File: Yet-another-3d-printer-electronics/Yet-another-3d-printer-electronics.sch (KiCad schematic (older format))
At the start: 14 parts, among them CON1 SD_Card, P2 BEDTEMP, P3 ENDTEMP, SW1 Switch_DPST, U2 LPC1114FBD48/302, X1 CRYSTAL_SMD

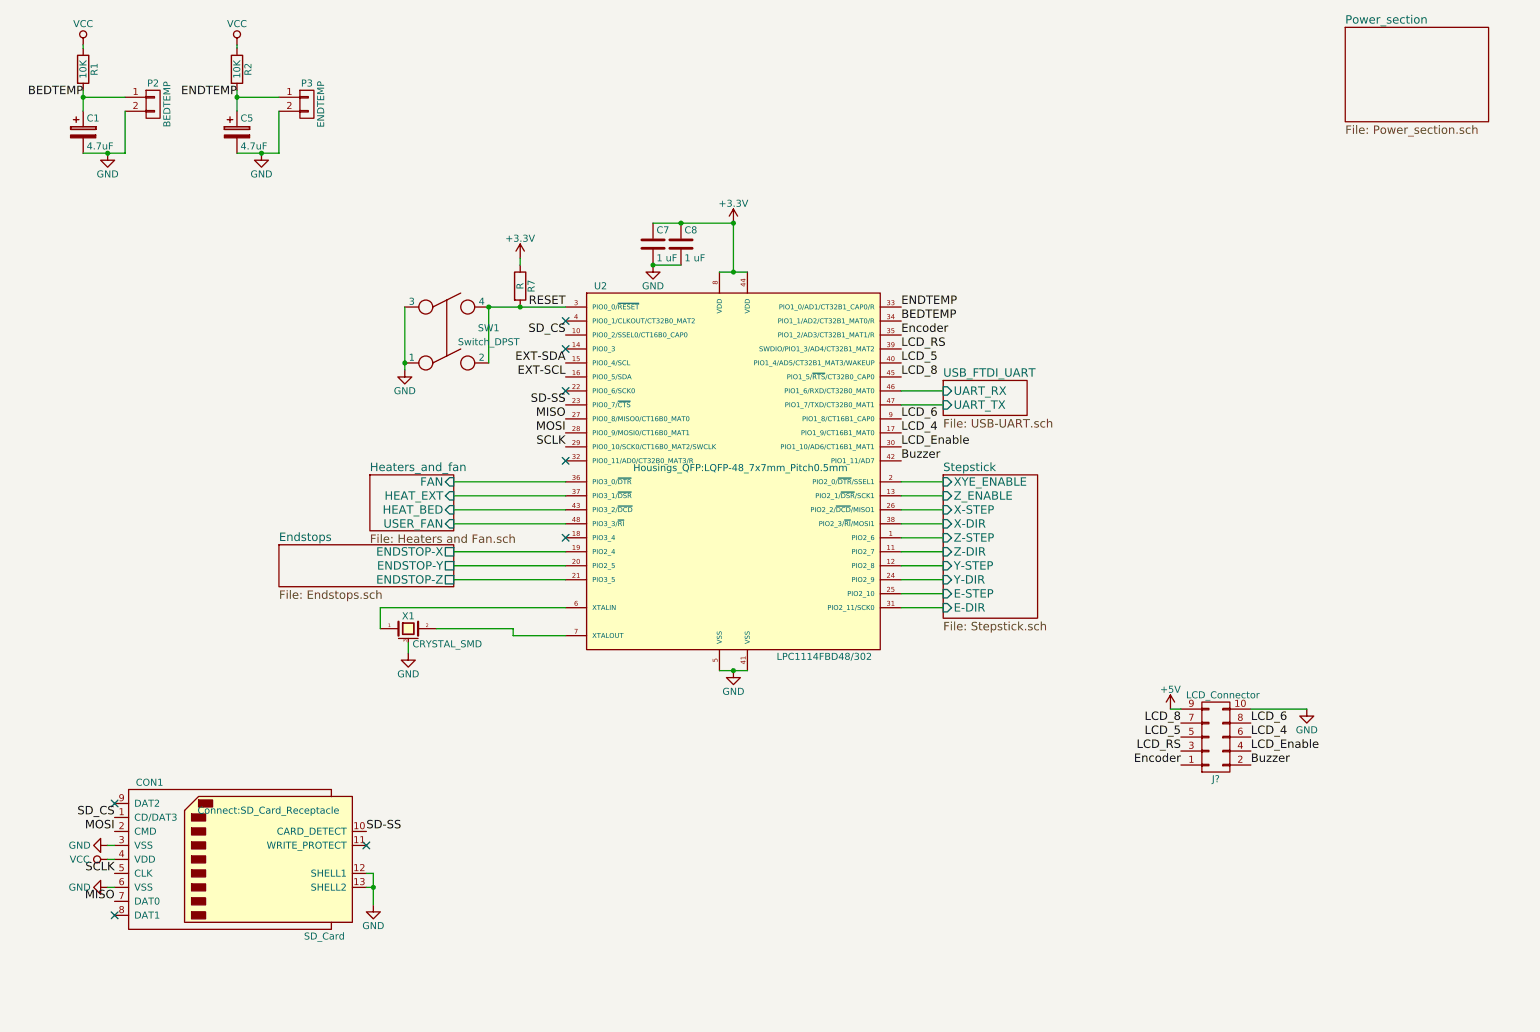
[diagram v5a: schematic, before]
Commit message: Add additional stepstick, hotend fan and heater and temperature sensor
Extruder stepsticks have independ enables pins. Vcc was replace by valid
power source.

Signed-off-by: Mateusz Krawczuk <mat.krawczuk@gmail.com>
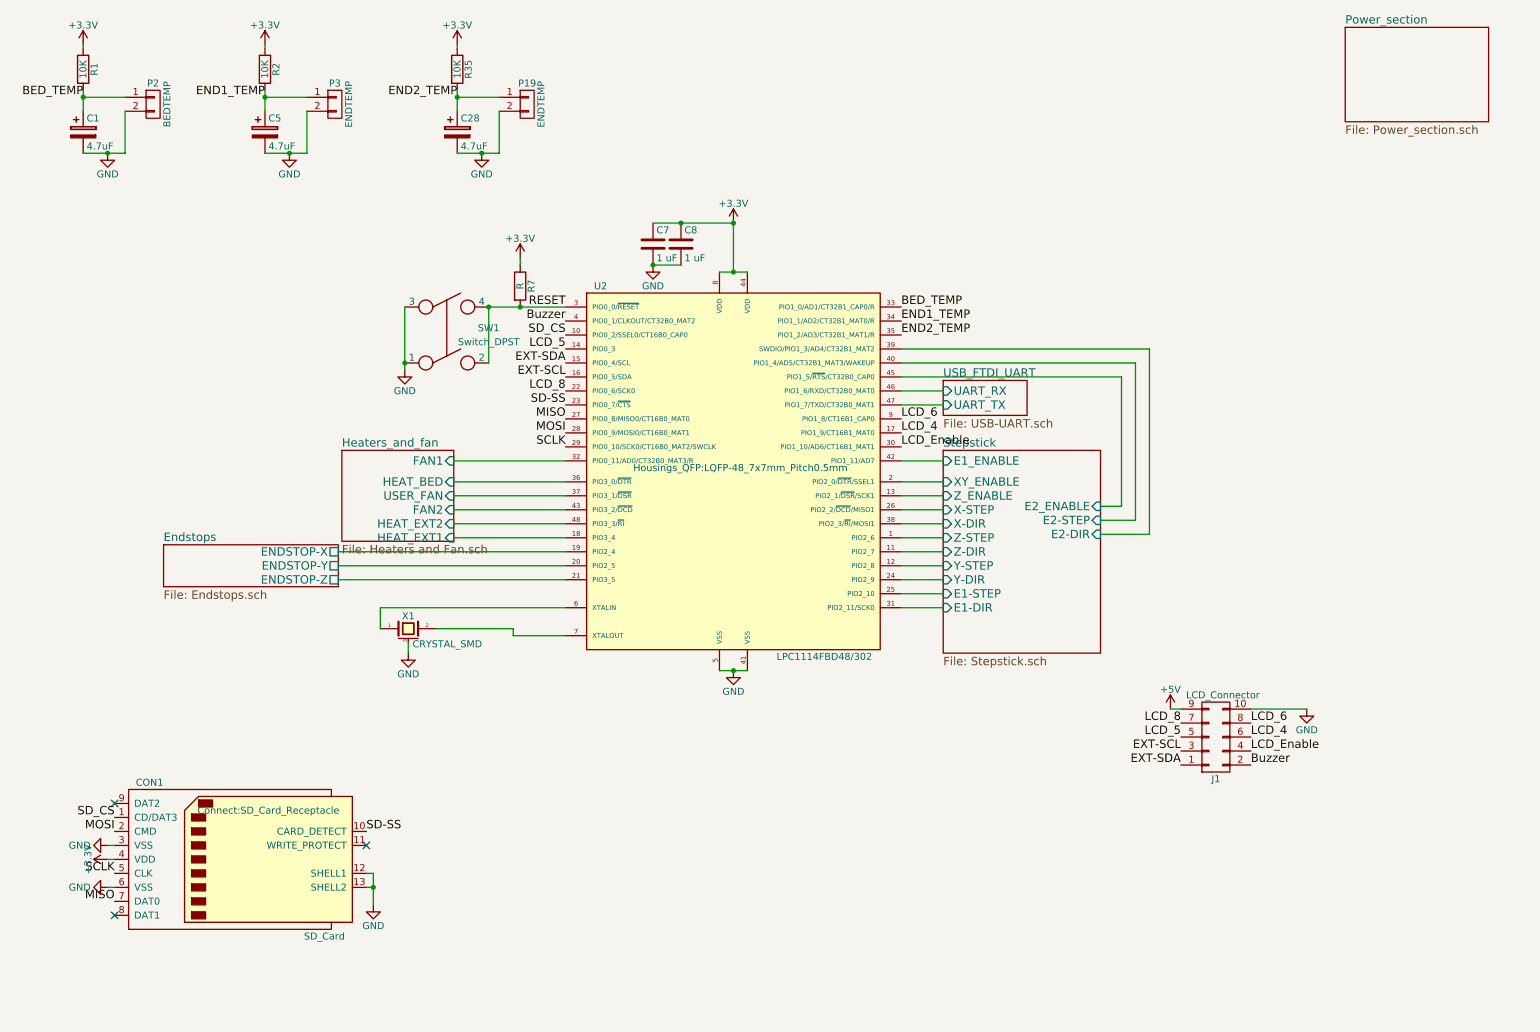
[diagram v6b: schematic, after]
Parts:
- added C28: 4.7uF, Capacitors_ThroughHole:CP_Radial_D4.0mm_P2.00mm, symbol CP
- added P19: ENDTEMP, Connectors_JST:JST_XH_B02B-XH-A_02x2.50mm_Straight, symbol CONN_01X02
- added R35: 10K, Resistors_SMD:R_0805_HandSoldering, symbol R
- gave numbers to parts that had none: 1
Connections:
- net Heaters_and_fan/FAN is gone; now on net Heaters_and_fan/HEAT_BED: U2.36 (PIO3_0/~DTR~)
- net Heaters_and_fan/HEAT_EXT is gone; now on net Heaters_and_fan/USER_FAN: U2.37 (PIO3_1/~DSR~)
- net VCC is gone; now on net +3V3: CON1.4 (VDD), R1.1, R2.1
- net +3V3: now also R35.1
- net Buzzer: now also U2.4 (PIO0_1/CLKOUT/CT32B0_MAT2); no longer U2.42 (PIO1_11/AD7)
- net EXT-SCL: now also J1.3 (P3)
- net EXT-SDA: now also J1.1 (P1)
- net GND: now also C28.2, P19.2 (P2)
- net Heaters_and_fan/HEAT_BED: no longer U2.43 (PIO3_2/~DCD~)
- net Heaters_and_fan/USER_FAN: no longer U2.48 (PIO3_3/~RI~)
- net LCD_5: now also U2.14 (PIO0_3); no longer U2.40 (PIO1_4/AD5/CT32B1_MAT3/WAKEUP)
- net LCD_8: now also U2.22 (PIO0_6/SCK0); no longer U2.45 (PIO1_5/~RTS~/CT32B0_CAP0)
- net Heaters_and_fan/HEAT_EXT1: now reaches U2.18 (PIO3_4)
- net Heaters_and_fan/FAN1: now reaches U2.32 (PIO0_11/AD0/CT32B0_MAT3/R)
- net BEDTEMP renamed BED_TEMP
- net BED_TEMP: now also U2.33 (PIO1_0/AD1/CT32B1_CAP0/R); no longer U2.34 (PIO1_1/AD2/CT32B1_MAT0/R)
- net ENDTEMP renamed END1_TEMP
- net END1_TEMP: now also U2.34 (PIO1_1/AD2/CT32B1_MAT0/R); no longer U2.33 (PIO1_0/AD1/CT32B1_CAP0/R)
- net Encoder renamed END2_TEMP
- net END2_TEMP: now also C28.1, P19.1 (P1), R35.2; no longer J1.1 (P1)
- net LCD_RS renamed Stepstick/E2-DIR
- net Stepstick/E2-DIR: no longer J1.3 (P3)
- net Stepstick/E-DIR renamed Stepstick/E1-DIR
- net Stepstick/E-STEP renamed Stepstick/E1-STEP
- net Stepstick/XYE_ENABLE renamed Stepstick/XY_ENABLE
- new net Heaters_and_fan/FAN2: U2.43 (PIO3_2/~DCD~)
- new net Heaters_and_fan/HEAT_EXT2: U2.48 (PIO3_3/~RI~)
- new net Stepstick/E1_ENABLE: U2.42 (PIO1_11/AD7)
- new net Stepstick/E2-STEP: U2.40 (PIO1_4/AD5/CT32B1_MAT3/WAKEUP)
- new net Stepstick/E2_ENABLE: U2.45 (PIO1_5/~RTS~/CT32B0_CAP0)
- no-connect marks 8 -> 3
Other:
- moved on the sheet: C5, P3, R2

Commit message: Add fuses to powersupply connector and heatbed.
TVS diode used to protect pins from short circuit. Correct connectors
names.

Signed-off-by: Mateusz Krawczuk <mat.krawczuk@gmail.com>
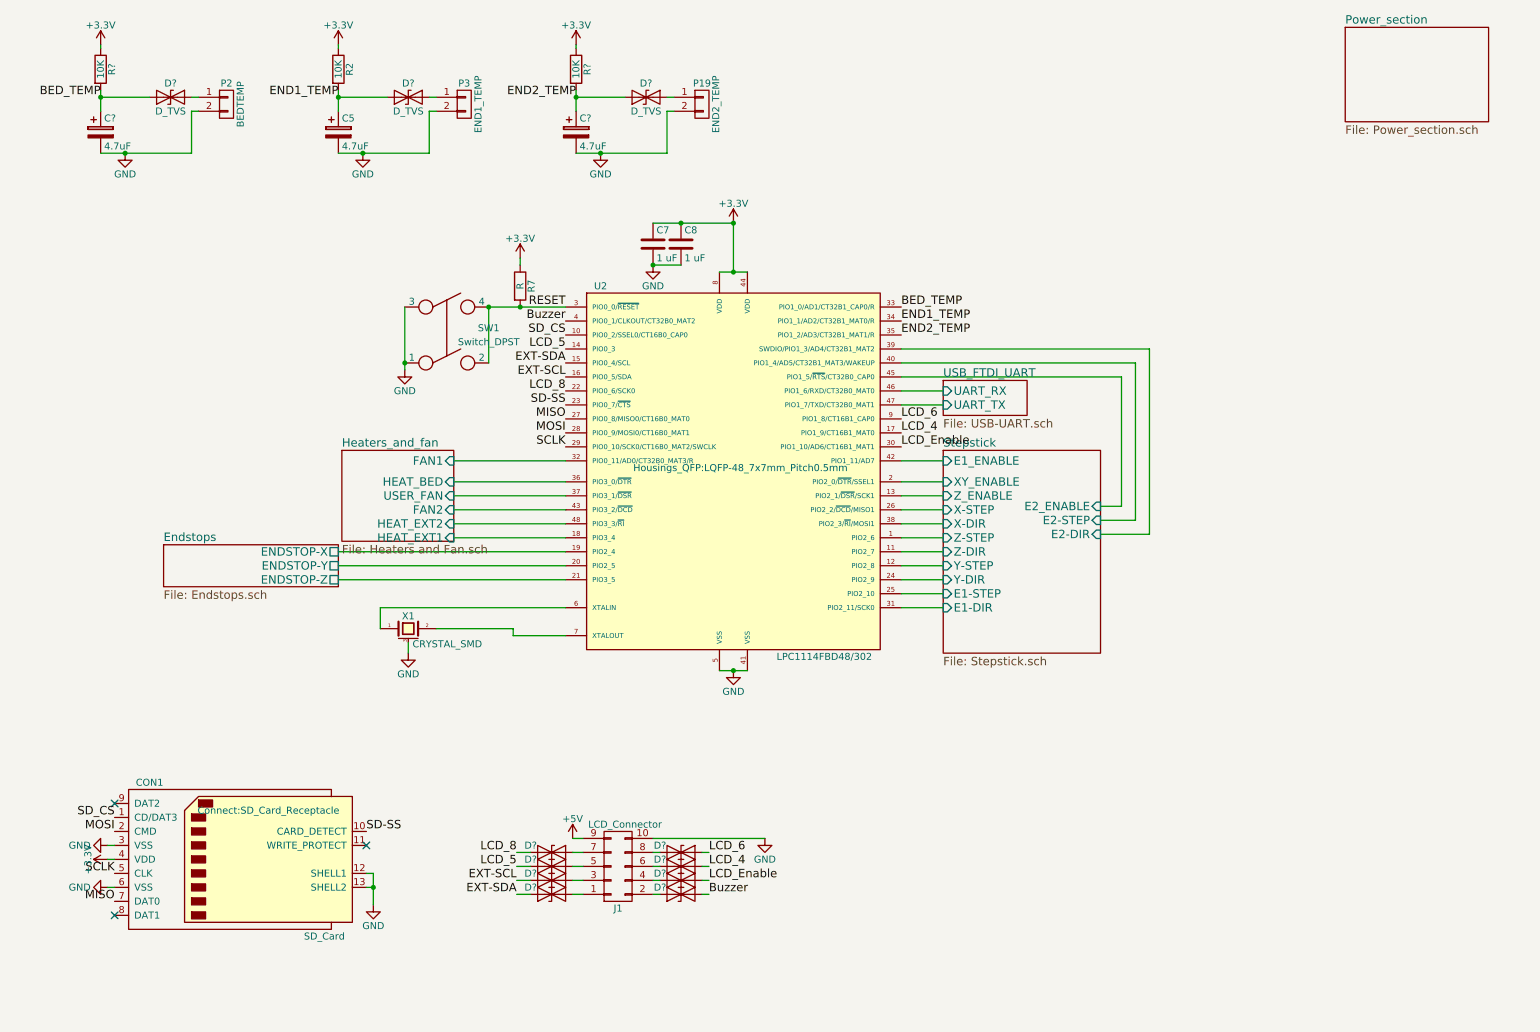
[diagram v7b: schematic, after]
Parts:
- removed C1: 4.7uF, Capacitors_ThroughHole:CP_Radial_D5.0mm_P2.00mm, symbol CP
- removed C28: 4.7uF, Capacitors_ThroughHole:CP_Radial_D4.0mm_P2.00mm, symbol CP
- removed R1, R35: 10K, Resistors_SMD:R_0805_HandSoldering, symbol R
- added C? (x2): 4.7uF, Capacitors_ThroughHole:CP_Radial_D4.0mm_P2.00mm, symbol CP
- added D? (x11): D_TVS, symbol D_TVS
- added R? (x2): 10K, Resistors_SMD:R_0805_HandSoldering, symbol R
- P19: value ENDTEMP -> END2_TEMP
- P3: value ENDTEMP -> END1_TEMP
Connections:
- net +3V3: now also R?.1, R?.1
- net BED_TEMP: now also C?.1, D?.1 (A1), R?.2; no longer P2.1 (P1)
- net Buzzer: now also D?.2 (A2); no longer J1.2 (P2)
- net END1_TEMP: now also D?.1 (A1); no longer P3.1 (P1)
- net END2_TEMP: now also C?.1, D?.1 (A1), R?.2; no longer P19.1 (P1)
- net EXT-SCL: now also D?.1 (A1); no longer J1.3 (P3)
- net EXT-SDA: now also D?.1 (A1); no longer J1.1 (P1)
- net GND: now also C?.2, C?.2
- net LCD_4: now also D?.2 (A2); no longer J1.6 (P6)
- net LCD_5: now also D?.1 (A1); no longer J1.5 (P5)
- net LCD_6: now also D?.2 (A2); no longer J1.8 (P8)
- net LCD_8: now also D?.1 (A1); no longer J1.7 (P7)
- net LCD_Enable: now also D?.2 (A2); no longer J1.4 (P4)
- new net: D?.2 (A2), P2.1 (P1)
- new net: D?.2 (A2), P3.1 (P1)
- new net: D?.2 (A2), J1.1 (P1)
- new net: D?.1 (A1), J1.2 (P2)
- new net: D?.2 (A2), J1.3 (P3)
- new net: D?.1 (A1), J1.4 (P4)
- new net: D?.2 (A2), J1.5 (P5)
- new net: D?.1 (A1), J1.6 (P6)
- new net: D?.2 (A2), J1.7 (P7)
- new net: D?.1 (A1), J1.8 (P8)
- new net: D?.2 (A2), P19.1 (P1)
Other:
- moved on the sheet: C5, J1, P19, P2, P3, R2
